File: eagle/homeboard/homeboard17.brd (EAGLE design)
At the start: 100 x 80 mm, 119 parts, among them IC1 XCF02S, IC2 25LC080SN, IC3 ATMEGA32U2-TQFP, Q5 BC848SMD, Q6 BC848SMD, Q7 BC848SMD, Q8 BC848SMD, T1 BSS138, T2 BC848, T3 BSS138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

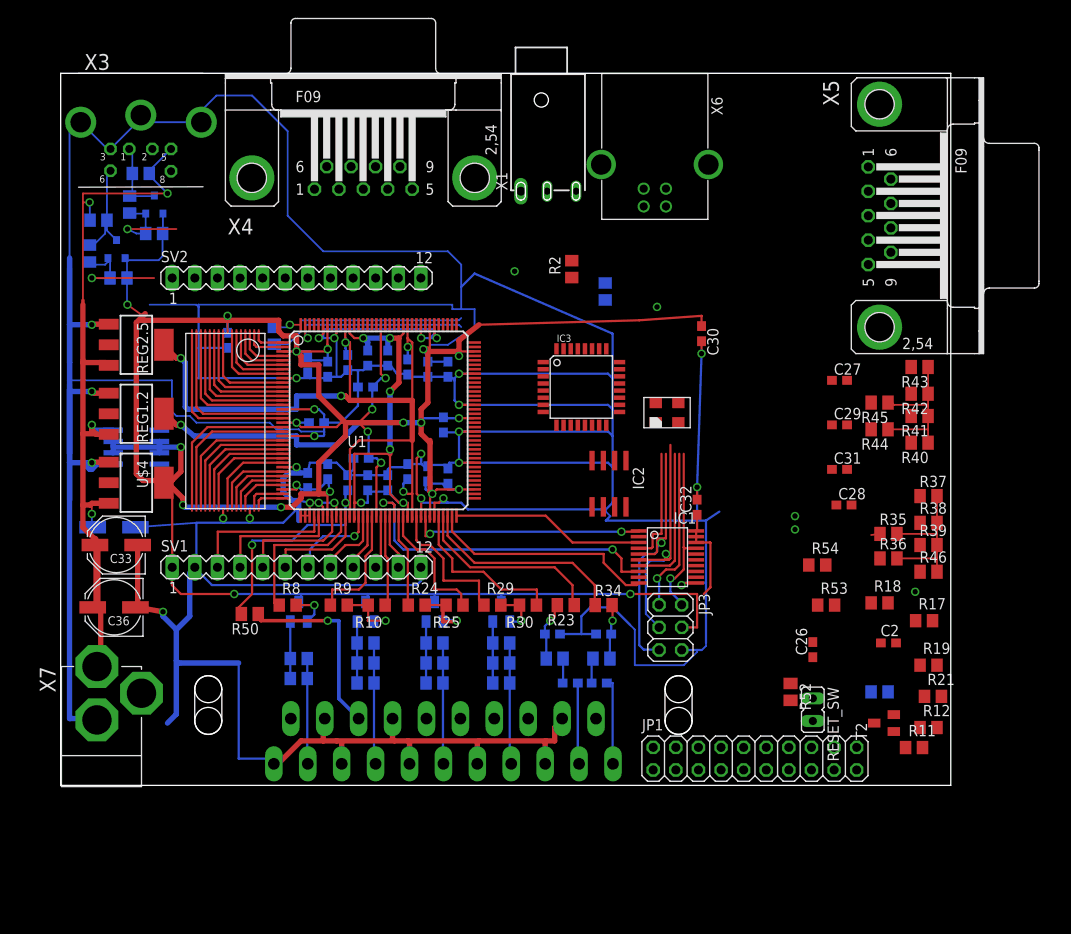
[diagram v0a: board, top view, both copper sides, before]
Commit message: got rid of dout/busy pin
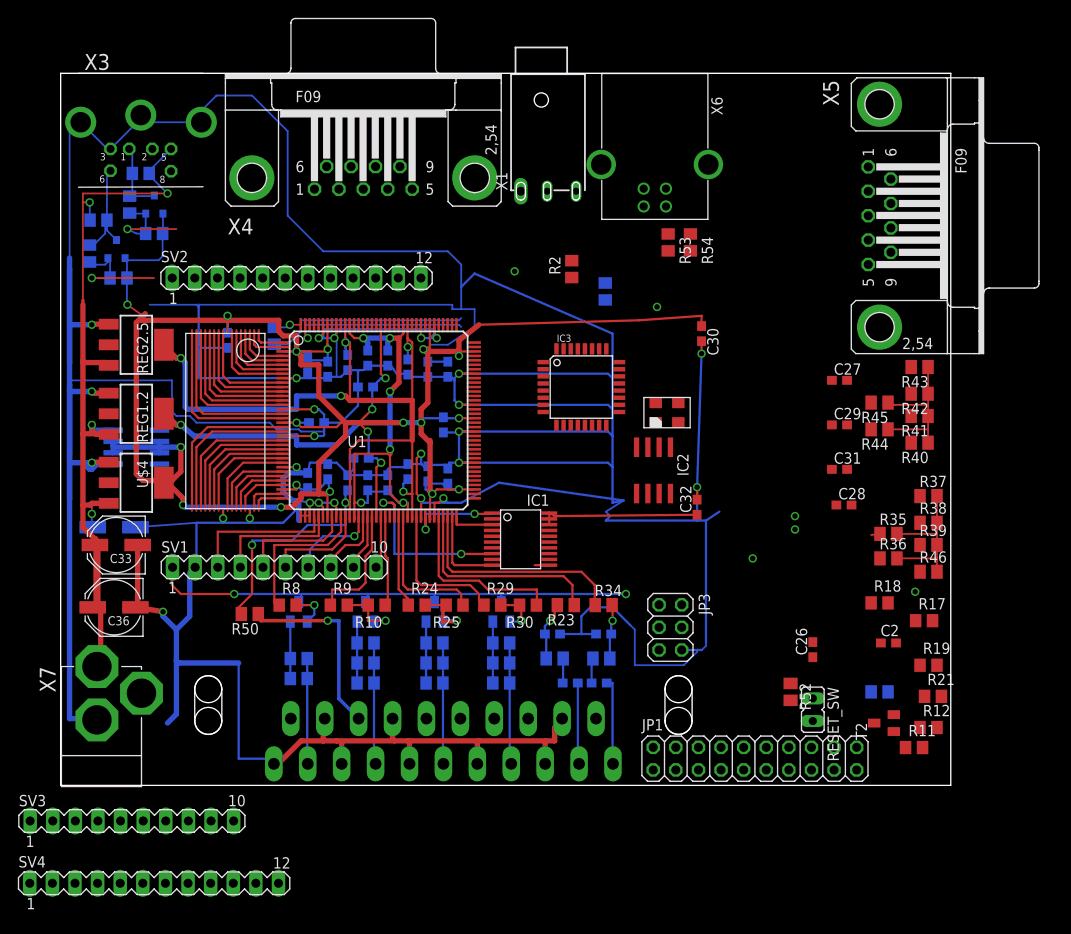
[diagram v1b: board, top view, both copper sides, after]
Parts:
- added SV3: (no value), con-lstb:MA10-1
- added SV4: (no value), con-lstb:MA12-1
- SV1: device con-lstb:MA12-1 -> con-lstb:MA10-1
- moved R53 44.4 mm to (68.2, 61.0), turned to 270 degrees
- moved R54 39.0 mm to (70.8, 61.0), turned to 270 degrees
- moved IC1 16.6 mm to (54.6, 24.7)
- moved IC2 5.22 mm to (66.6, 35.4)
- moved SV1 2.50 mm to (24.0, 24.5)
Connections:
- removed net XXZXZ: SV1.11, U1.P57
- net GND: no longer SV1.12
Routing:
- net TMS: track 30.4 -> 0.06 mm, vias 1 -> 0
- net TCK: track 28.1 -> 0.00 mm, vias 1 -> 0
- net GND: track 808.5 -> 782.0 mm
- net TDO_PROM: track 20.0 -> 0.00 mm, vias 1 -> 0
- net TDO_EXP: track 18.7 -> 0.00 mm, vias 1 -> 0
- net PROM_INITB: track 37.7 -> 20.4 mm
- net N$35: track 21.7 -> 4.97 mm
- net N$40: track 37.1 -> 20.8 mm
- net N$38: track 25.9 -> 9.86 mm
- net PROM_DO: track 26.7 -> 10.9 mm
- net VCC: track 402.1 -> 387.9 mm
- net TDO_FPGA: track 13.1 -> 0.00 mm
- net XXZXZ: track 6.23 -> 0.00 mm
- net FPGA_AUDIO_RIGHT: track 23.4 -> 25.4 mm
- net FPGA_AUDIO_LEFT: track 21.7 -> 23.8 mm
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
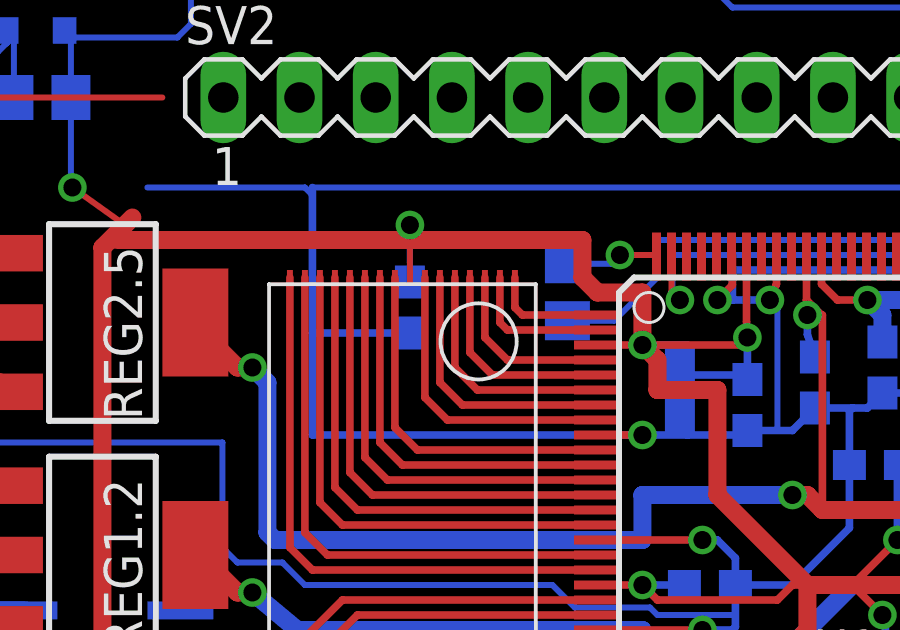
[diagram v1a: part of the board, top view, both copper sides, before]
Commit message: moved ram cap down
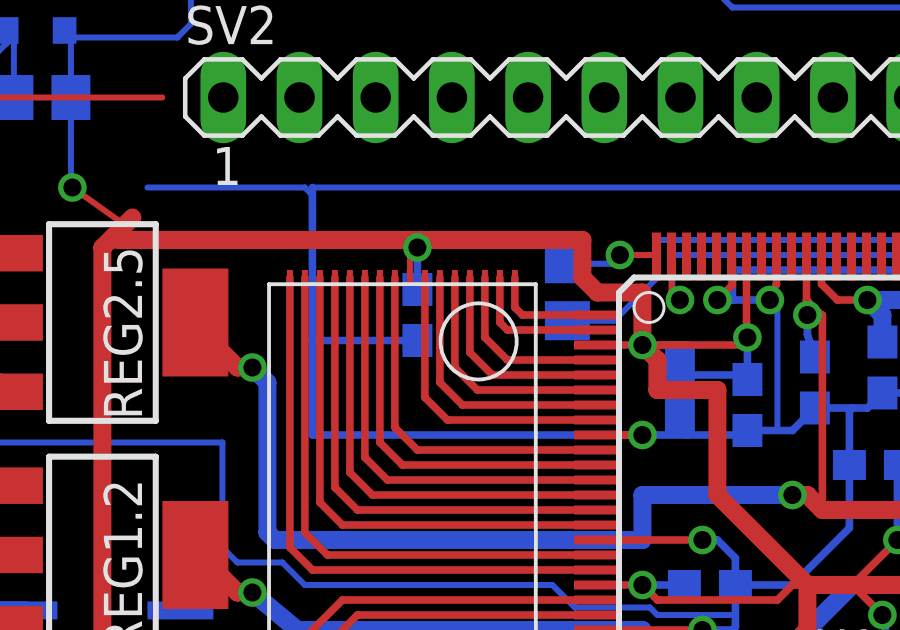
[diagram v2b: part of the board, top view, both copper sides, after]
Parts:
- moved C34 0.35 mm to (19.0, 49.8)
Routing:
- net VCC: track 387.9 -> 386.2 mm
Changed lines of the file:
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@@
 <element name="U$5" library="cpcfpga" package="SO8" value="MC33269D" x="8.5" y="38" rot="MR90"/>
 <element name="U$6" library="cpcfpga" package="TSOP32" value="AS6C4008" x="18.5" y="41.25" rot="R270"/>
-<element name="C34" library="rcl" package="C0603" value="100nF" x="18.75" y="50" rot="MR270"/>
+<element name="C34" library="rcl" package="C0603" value="100nF" x="19" y="49.75" rot="MR270"/>
 <element name="C35" library="rcl" package="PANASONIC_D" value="100u" x="6" y="29" rot="MR0"/>
 <element name="C36" library="rcl" package="PANASONIC_D" value="100u" x="6" y="20" rot="R180"/>
@@
 <wire x1="33.4" y1="46.55" x2="33.5" y2="46.65" width="0.254" layer="16"/>
 <wire x1="15.5" y1="45.75" x2="26.5" y2="45.75" width="0.254" layer="16"/>
-<wire x1="15.5" y1="45.75" x2="15.5" y2="49.15" width="0.254" layer="16"/>
-<wire x1="15.5" y1="49.15" x2="15.5" y2="53.75" width="0.254" layer="16"/>
+<wire x1="15.5" y1="45.75" x2="15.5" y2="48.9" width="0.254" layer="16"/>
+<wire x1="15.5" y1="48.9" x2="15.5" y2="53.75" width="0.254" layer="16"/>
 <wire x1="15.5" y1="54" x2="15.5" y2="53.75" width="0.254" layer="16"/>
 <wire x1="42" y1="51.25" x2="29.5" y2="51.25" width="0.254" layer="16"/>
@@
 <wire x1="26.75" y1="30.75" x2="26.5" y2="31" width="0.254" layer="16"/>
 <wire x1="15.25" y1="24.64" x2="14.5" y2="23.89" width="0.254" layer="16"/>
-<wire x1="18.75" y1="49.15" x2="15.5" y2="49.15" width="0.254" layer="16"/>
+<wire x1="19" y1="48.9" x2="15.5" y2="48.9" width="0.254" layer="16"/>
 <wire x1="1" y1="59.25" x2="1" y2="73.5" width="0.2" layer="16"/>
 <wire x1="1" y1="73.5" x2="2" y2="74.5" width="0.2" layer="16"/>
@@
 <wire x1="15.11" y1="24.5" x2="15.25" y2="24.64" width="0" layer="19" extent="16-16"/>
 <wire x1="41.97" y1="30.3" x2="42" y2="29.825" width="0" layer="19" extent="1-1"/>
-<wire x1="64.698553125" y1="37.9890875" x2="61.5" y2="36.25" width="0" layer="19" extent="1-16"/>
+<wire x1="64.698553125" y1="37.9890875" x2="62" y2="39.25" width="0" layer="19" extent="1-16"/>
 <wire x1="51" y1="57.75" x2="46.5" y2="57.5" width="0" layer="19" extent="16-16"/>
+<wire x1="69.395" y1="40.775" x2="64.698553125" y2="37.9890875" width="0" layer="19" extent="1-1"/>
 <wire x1="67" y1="53.75" x2="62" y2="50.75" width="0" layer="19" extent="16-16"/>
 <wire x1="21.4778" y1="68.25" x2="25.5" y2="64" width="0" layer="19" extent="16-16"/>
+<wire x1="54.893396875" y1="24.737409375" x2="59.5" y2="20" width="0" layer="19" extent="1-16"/>
 <wire x1="54.2074" y1="45.95" x2="61.5" y2="46.25" width="0" layer="19" extent="1-16"/>
-<wire x1="54.893396875" y1="24.737409375" x2="59.5" y2="20" width="0" layer="19" extent="1-16"/>
-<wire x1="69.395" y1="40.775" x2="62" y2="39.25" width="0" layer="19" extent="1-16"/>
 <wire x1="51.7" y1="66.75" x2="51" y2="57.75" width="0" layer="19" extent="1-1"/>
 <wire x1="35.3716" y1="69.52" x2="25.5" y2="73.5" width="0" layer="19" extent="16-16"/>
@@
 <wire x1="27" y1="40.25" x2="26.5" y2="40.75" width="0.254" layer="1"/>
 <wire x1="27.9" y1="40.75" x2="26.5" y2="40.75" width="0.254" layer="16"/>
-<wire x1="24.5" y1="52.25" x2="18.75" y2="52.25" width="0.6" layer="1"/>
+<wire x1="24.5" y1="52.25" x2="19" y2="52.25" width="0.6" layer="1"/>
 <contactref element="C34" pad="1"/>
 <contactref element="U$5" pad="2"/>
@@
 <contactref element="U$5" pad="3"/>
 <contactref element="U$5" pad="6"/>
+<wire x1="19" y1="52.25" x2="18.75" y2="52.25" width="0.6" layer="1"/>
 <wire x1="18.75" y1="52.25" x2="9" y2="52.25" width="0.6" layer="1"/>
 <wire x1="5.9" y1="38.635" x2="5.9" y2="37.365" width="0.6096" layer="16"/>
@@
 <wire x1="49.5" y1="20.6" x2="49.5" y2="21.5" width="0.254" layer="16"/>
 <wire x1="18.75" y1="51" x2="18.75" y2="52.25" width="0.2" layer="1"/>
-<via x="18.75" y="52.75" extent="1-16" drill="0.6" shape="square"/>
-<wire x1="18.75" y1="52.75" x2="18.75" y2="51.5" width="0.2" layer="16"/>
-<wire x1="18.75" y1="50.85" x2="18.75" y2="52.75" width="0.2" layer="16"/>
-<wire x1="18.75" y1="52.25" x2="18.75" y2="52.75" width="0.2" layer="1"/>
+<via x="19" y="52" extent="1-16" drill="0.6" shape="square"/>
+<wire x1="18.75" y1="52.25" x2="19" y2="52" width="0.2" layer="1"/>
 <wire x1="11.4906" y1="64.234" x2="11.4906" y2="62.0406" width="0.2" layer="16"/>
 <wire x1="11.4906" y1="62.0406" x2="11.45" y2="62" width="0.2" layer="16"/>
@@
 <wire x1="7.45" y1="59.0246" x2="7.2406" y2="59.234" width="0.2" layer="16"/>
 <contactref element="SV1" pad="1"/>
+<wire x1="19" y1="52" x2="19" y2="50.6" width="0.254" layer="16"/>
+<wire x1="19" y1="52" x2="19" y2="52.25" width="0.254" layer="1"/>
 <wire x1="98.45" y1="32.5" x2="97.45" y2="38.5" width="0" layer="19" extent="1-1"/>
 <wire x1="86.65" y1="40.5" x2="92.95" y2="40" width="0" layer="19" extent="1-1"/>
@@
 <wire x1="55.7" y1="49.0426" x2="54.2074" y2="45.15" width="0" layer="19" extent="1-1"/>
 <wire x1="56.5" y1="49.0426" x2="55.7" y2="49.0426" width="0" layer="19" extent="1-1"/>
-<wire x1="54.893396875" y1="30.643396875" x2="46.42" y2="33.25" width="0" layer="19" extent="1-1"/>
+<wire x1="54.893396875" y1="30.587409375" x2="46.42" y2="33.25" width="0" layer="19" extent="1-1"/>
 <wire x1="68.508553125" y1="32.7890875" x2="71.5" y2="30.4" width="0" layer="19" extent="1-1"/>
 <wire x1="66.855" y1="42.975" x2="65" y2="52.25" width="0" layer="19" extent="1-1"/>
@@
 <contactref element="IC3" pad="30"/>
 <contactref element="R53" pad="2"/>
-<wire x1="68.25" y1="60.05" x2="57.3" y2="49.0426" width="0" layer="19" extent="1-1"/>
+<wire x1="57.3" y1="49.0426" x2="68.25" y2="60.05" width="0" layer="19" extent="1-1"/>
 </signal>
 <signal name="N$49">

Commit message: mah
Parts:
- removed SV2, SV4: (no value), con-lstb:MA12-1
- moved SV3 63.1 mm to (24.0, 57.0)
- moved IC1 4.50 mm to (59.1, 24.7)
- moved IC3 4.32 mm to (57.8, 40.5), turned to 270 degrees
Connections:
- net TDI_FPGA: now also IC3.21; no longer IC3.20
- net TDO_EXP: now also IC3.22; no longer IC3.21
- net TDO_PROM: now also IC3.20; no longer IC3.22
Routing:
- net PS2DAT: track 11.8 -> 37.3 mm
- net PS2CLK: track 14.1 -> 36.5 mm
- net N$40: track 20.8 -> 30.7 mm
- net TCK: track 0.00 -> 8.83 mm
- net TMS: track 0.06 -> 7.83 mm
- net VCC: track 386.2 -> 380.8 mm
- net PROM_INITB: track 20.4 -> 24.9 mm
- net PROM_DO: track 10.9 -> 15.4 mm
- net N$38: track 9.86 -> 14.4 mm
- net N$35: track 4.97 -> 9.47 mm
- net TDO_FPGA: track 0.00 -> 2.21 mm

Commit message: mah
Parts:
- moved SV3 2.00 mm to (24.0, 59.0)
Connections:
- removed net XXCSYNC: U1.P137
- new net N$1: SV3.3, U1.P137
- new net N$2: SV3.4, U1.P135
- new net N$3: SV3.5, U1.P132
- new net N$4: SV3.6, U1.P131
- new net N$5: SV3.7, U1.P130
- new net N$6: SV3.8, U1.P129
- new net N$7: SV3.9, U1.P128
- new net N$8: SV3.10, U1.P127
- net GND: now also SV3.2
- net VCC: now also SV3.1
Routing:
- net N$1: track 0.00 -> 19.4 mm
- net N$2: track 0.00 -> 17.7 mm
- net N$3: track 0.00 -> 16.1 mm
- net N$4: track 0.00 -> 13.6 mm
- net N$5: track 0.00 -> 11.9 mm
- net N$6: track 0.00 -> 9.89 mm
- net N$7: track 0.00 -> 8.16 mm
- net N$8: track 0.00 -> 7.32 mm
- net GND: track 782.2 -> 787.4 mm
- net VCC: track 380.8 -> 383.0 mm
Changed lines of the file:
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@@
 <element name="JP1" library="pinhead" package="2X10" value="" x="78" y="3"/>
 <element name="X7" library="powersupply" package="DC-21MM" value="DC21MMX" x="4" y="7" rot="R180"/>
-<element name="SV3" library="con-lstb" package="MA10-1" value="" x="24" y="57">
-<attribute name="OC_NEWARK" value="unknown" x="24" y="57" size="1.778" layer="27" display="off"/>
-<attribute name="MPN" value="" x="24" y="57" size="1.778" layer="27" display="off"/>
-<attribute name="MF" value="" x="24" y="57" size="1.778" layer="27" display="off"/>
-<attribute name="OC_FARNELL" value="unknown" x="24" y="57" size="1.778" layer="27" display="off"/>
+<element name="SV3" library="con-lstb" package="MA10-1" value="" x="24" y="59">
+<attribute name="OC_NEWARK" value="unknown" x="24" y="59" size="1.778" layer="27" display="off"/>
+<attribute name="MPN" value="" x="24" y="59" size="1.778" layer="27" display="off"/>
+<attribute name="MF" value="" x="24" y="59" size="1.778" layer="27" display="off"/>
+<attribute name="OC_FARNELL" value="unknown" x="24" y="59" size="1.778" layer="27" display="off"/>
 </element>
 <element name="SV1" library="con-lstb" package="MA10-1" value="" x="24" y="24.5">
@@
 <wire x1="15.5" y1="53.75" x2="15.25" y2="54" width="0.2" layer="16"/>
 <wire x1="15.25" y1="54" x2="10" y2="54" width="0.2" layer="16"/>
-<wire x1="43.5" y1="60" x2="45" y2="58.5" width="0.2" layer="16"/>
-<wire x1="43.5" y1="60" x2="29.5" y2="60" width="0.2" layer="16"/>
-<wire x1="29.5" y1="60" x2="25.5" y2="64" width="0.2" layer="16"/>
+<wire x1="41.5" y1="62" x2="45" y2="58.5" width="0.2" layer="16"/>
+<wire x1="41.5" y1="62" x2="27.5" y2="62" width="0.2" layer="16"/>
+<wire x1="27.5" y1="62" x2="25.5" y2="64" width="0.2" layer="16"/>
 <wire x1="25.5" y1="64" x2="25.5" y2="73.5" width="0.2" layer="16"/>
 <wire x1="25.5" y1="73.5" x2="21.5" y2="77.5" width="0.2" layer="16"/>
@@
 <wire x1="61.25" y1="30.75" x2="61.75" y2="30.25" width="0.2" layer="16"/>
 <contactref element="SV1" pad="2"/>
+<contactref element="SV3" pad="2"/>
+<wire x1="15.11" y1="59" x2="15.11" y2="54.39" width="0.254" layer="16"/>
+<wire x1="15.11" y1="54.39" x2="15.5" y2="54" width="0.254" layer="16"/>
 <wire x1="93.27" y1="62.6284" x2="92" y2="76.5222" width="0" layer="19" extent="1-1"/>
 <wire x1="88.35" y1="45.5" x2="93.27" y2="62.6284" width="0" layer="19" extent="1-1"/>
@@
 <wire x1="21.4778" y1="68.25" x2="25.5" y2="64" width="0" layer="19" extent="16-16"/>
 <wire x1="51.7" y1="66.75" x2="51" y2="57.75" width="0" layer="19" extent="1-1"/>
-<wire x1="35.3716" y1="69.52" x2="25.5" y2="73.5" width="0" layer="19" extent="16-16"/>
+<wire x1="35.3716" y1="69.52" x2="41.5" y2="62" width="0" layer="19" extent="16-16"/>
 <wire x1="66.57" y1="1.73" x2="55.5" y2="5" width="0" layer="19" extent="1-1"/>
 <wire x1="84.5" y1="16.1" x2="77.75" y2="25.5" width="0" layer="19" extent="1-1"/>
@@
 <wire x1="8.5" y1="53" x2="8" y2="53.5" width="0.254" layer="1"/>
 <wire x1="8" y1="53.5" x2="7.5" y2="54" width="0.254" layer="1"/>
+<contactref element="SV3" pad="1"/>
+<wire x1="12.57" y1="59" x2="12.5" y2="59" width="0.254" layer="16"/>
+<wire x1="12.5" y1="59" x2="11" y2="60.5" width="0.254" layer="16"/>
 <wire x1="98.45" y1="32.5" x2="97.45" y2="38.5" width="0" layer="19" extent="1-1"/>
 <wire x1="86.65" y1="40.5" x2="92.95" y2="40" width="0" layer="19" extent="1-1"/>
@@
 <wire x1="44.75" y1="52.25" x2="45" y2="52.5" width="0.2" layer="16"/>
 <contactref element="IC3" pad="21"/>
-<wire x1="58.15" y1="36.2074" x2="56.7926" y2="34.7074" width="0" layer="19" extent="1-16"/>
-<wire x1="56.7926" y1="34.7074" x2="57" y2="34.5" width="0" layer="19" extent="1-16"/>
 <wire x1="44.75" y1="52.25" x2="58.15" y2="36.2074" width="0" layer="19" extent="1-16"/>
 </signal>
@@
 <contactref element="U$2" pad="OUT"/>
 </signal>
-<signal name="XXB1">
-</signal>
-<signal name="XXB0">
-</signal>
-<signal name="XXG0">
-</signal>
-<signal name="XXCSYNC">
-<contactref element="U1" pad="P137"/>
-</signal>
 <signal name="FL_HOLD">
 <contactref element="IC2" pad="7"/>
@@
 <wire x1="32.89" y1="24.5" x2="33" y2="24.5" width="0" layer="19" extent="1-1"/>
 </signal>
+<signal name="N$1">
+<contactref element="SV3" pad="3"/>
+<contactref element="U1" pad="P137"/>
+<wire x1="30.47" y1="51.7" x2="30.47" y2="53.53" width="0.254" layer="1"/>
+<wire x1="30.47" y1="53.53" x2="29.5" y2="54.5" width="0.254" layer="1"/>
+<wire x1="29.5" y1="54.5" x2="18" y2="54.5" width="0.254" layer="1"/>
+<wire x1="18" y1="54.5" x2="17.5" y2="55" width="0.254" layer="1"/>
+<wire x1="17.5" y1="55" x2="17.5" y2="59" width="0.254" layer="1"/>
+<wire x1="17.5" y1="59" x2="17.65" y2="59" width="0" layer="19" extent="1-16"/>
+</signal>
+<signal name="N$2">
+<contactref element="SV3" pad="4"/>
+<contactref element="U1" pad="P135"/>
+<wire x1="31.47" y1="51.7" x2="31.47" y2="53.53" width="0.254" layer="1"/>
+<wire x1="31.47" y1="53.53" x2="30" y2="55" width="0.254" layer="1"/>
+<wire x1="30" y1="55" x2="20.5" y2="55" width="0.254" layer="1"/>
+<wire x1="20.5" y1="55" x2="20" y2="55.5" width="0.254" layer="1"/>
+<wire x1="20" y1="55.5" x2="20" y2="58.81" width="0.254" layer="1"/>
+<wire x1="20" y1="58.81" x2="20.19" y2="59" width="0.254" layer="1"/>
+</signal>
+<signal name="N$3">
+<contactref element="SV3" pad="5"/>
+<contactref element="U1" pad="P132"/>
+<wire x1="32.97" y1="51.7" x2="32.97" y2="53.03" width="0.254" layer="1"/>
+<wire x1="32.97" y1="53.03" x2="30.5" y2="55.5" width="0.254" layer="1"/>
+<wire x1="30.5" y1="55.5" x2="23" y2="55.5" width="0.254" layer="1"/>
+<wire x1="23" y1="55.5" x2="22.5" y2="56" width="0.254" layer="1"/>
+<wire x1="22.5" y1="56" x2="22.5" y2="58.77" width="0.254" layer="1"/>
+<wire x1="22.5" y1="58.77" x2="22.73" y2="59" width="0.254" layer="1"/>
+</signal>
+<signal name="N$4">
+<contactref element="SV3" pad="6"/>
+<contactref element="U1" pad="P131"/>
+<wire x1="33.47" y1="51.7" x2="33.47" y2="53.53" width="0.254" layer="1"/>
+<wire x1="33.47" y1="53.53" x2="31" y2="56" width="0.254" layer="1"/>
+<wire x1="31" y1="56" x2="26" y2="56" width="0.254" layer="1"/>
+<wire x1="26" y1="56" x2="25.5" y2="56.5" width="0.254" layer="1"/>
+<wire x1="25.5" y1="56.5" x2="25.5" y2="58.77" width="0.254" layer="1"/>
+<wire x1="25.5" y1="58.77" x2="25.27" y2="59" width="0.254" layer="1"/>
+</signal>
+<signal name="N$5">
+<contactref element="SV3" pad="7"/>
+<contactref element="U1" pad="P130"/>
+<wire x1="33.97" y1="51.7" x2="33.97" y2="54.03" width="0.254" layer="1"/>
+<wire x1="33.97" y1="54.03" x2="31.5" y2="56.5" width="0.254" layer="1"/>
+<wire x1="31.5" y1="56.5" x2="28" y2="56.5" width="0.254" layer="1"/>
+<wire x1="28" y1="56.5" x2="28" y2="58.81" width="0.254" layer="1"/>
+<wire x1="28" y1="58.81" x2="27.81" y2="59" width="0.254" layer="1"/>
+</signal>
+<signal name="N$6">
+<contactref element="SV3" pad="8"/>
+<contactref element="U1" pad="P129"/>
+<wire x1="34.47" y1="51.7" x2="34.47" y2="54.53" width="0.254" layer="1"/>
+<wire x1="34.47" y1="54.53" x2="32" y2="57" width="0.254" layer="1"/>
+<wire x1="32" y1="57" x2="30.5" y2="57" width="0.254" layer="1"/>
+<wire x1="30.5" y1="57" x2="30.5" y2="58.85" width="0.254" layer="1"/>
+<wire x1="30.5" y1="58.85" x2="30.35" y2="59" width="0.254" layer="1"/>
+</signal>
+<signal name="N$7">
+<contactref element="SV3" pad="9"/>
+<contactref element="U1" pad="P128"/>
+<wire x1="34.97" y1="51.7" x2="34.97" y2="55.03" width="0.254" layer="1"/>
+<wire x1="34.97" y1="55.03" x2="33" y2="57" width="0.254" layer="1"/>
+<wire x1="33" y1="57" x2="33" y2="58.89" width="0.254" layer="1"/>
+<wire x1="33" y1="58.89" x2="32.89" y2="59" width="0.254" layer="1"/>
+</signal>
+<signal name="N$8">
+<contactref element="SV3" pad="10"/>
+<contactref element="U1" pad="P127"/>
+<wire x1="35.47" y1="51.7" x2="35.47" y2="58.96" width="0.254" layer="1"/>
+<wire x1="35.47" y1="58.96" x2="35.43" y2="59" width="0.254" layer="1"/>
+</signal>
 </signals>
